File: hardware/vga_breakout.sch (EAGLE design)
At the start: 11 parts, among them J1 VGA_DB15, J2 HEADER_5P

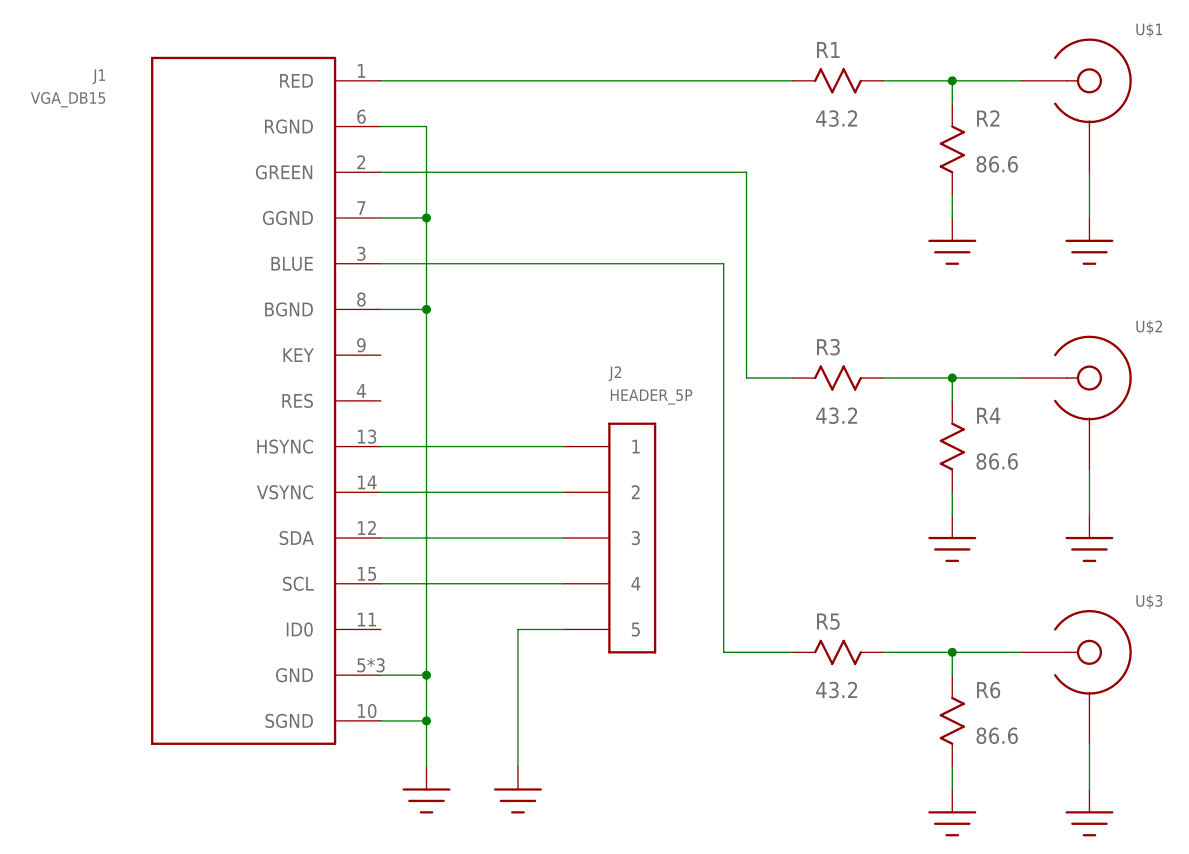
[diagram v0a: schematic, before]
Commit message: added +5V line to breakout PCB
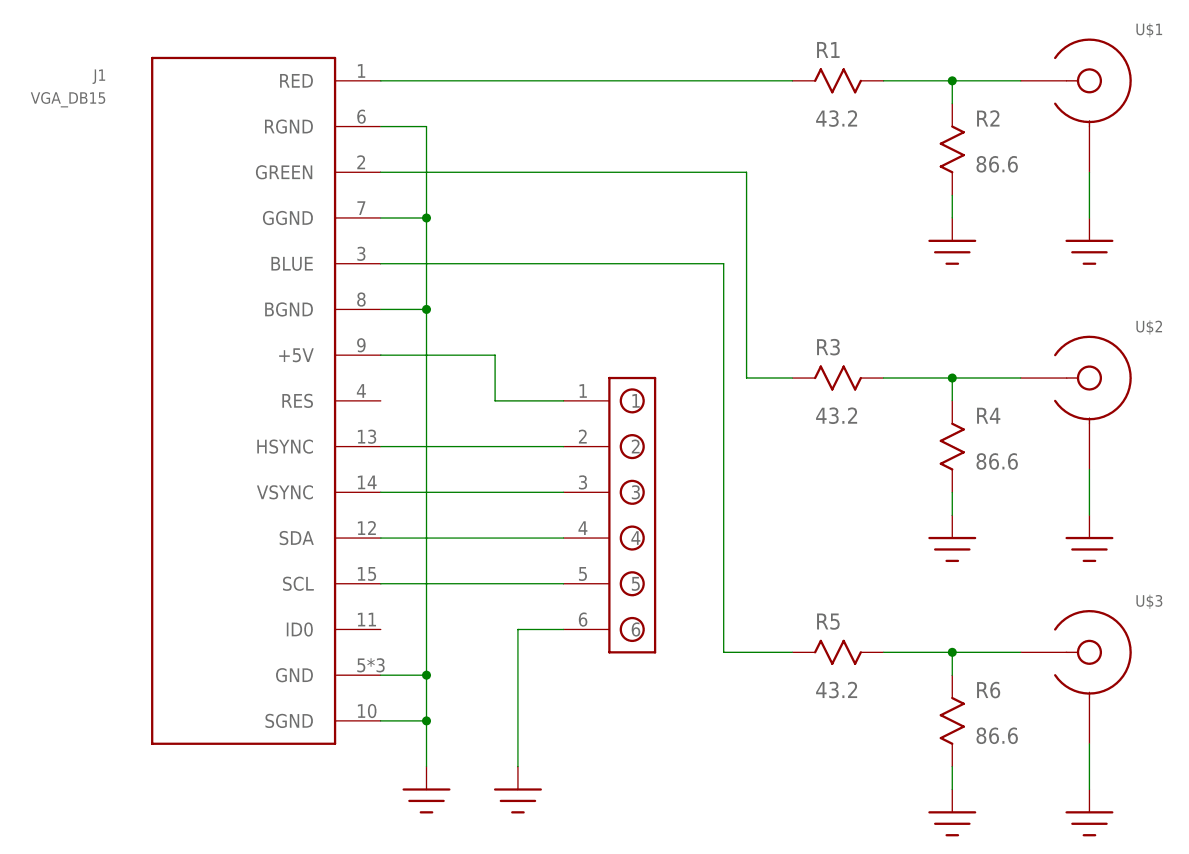
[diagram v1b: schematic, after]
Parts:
- removed J2: HEADER_5P, mw-voice-marker:HEADER_5P
- added U$9: HEADER_6P, mw-voice-marker:HEADER_6P
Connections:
- new net +5V: J1.+5V, U$9.1
- net GND: now also U$9.6; no longer J2.5
- net HSYNC: now also U$9.2; no longer J2.1
- net SCL: now also U$9.5; no longer J2.4
- net SDA: now also U$9.4; no longer J2.3
- net VSYNC: now also U$9.3; no longer J2.2
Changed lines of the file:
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@@
 <part name="U$16" library="mw-voice-marker" deviceset="GND" device=""/>
 <part name="U$17" library="mw-voice-marker" deviceset="GND" device=""/>
-<part name="J2" library="mw-voice-marker" deviceset="HEADER_5P" device=""/>
+<part name="U$9" library="mw-voice-marker" deviceset="HEADER_6P" device=""/>
 </parts>
 <sheets>
@@
 <instance part="U$16" gate="G$1" x="71.12" y="40.64"/>
 <instance part="U$17" gate="G$1" x="71.12" y="10.16"/>
-<instance part="J2" gate="G$1" x="35.56" y="38.1"/>
+<instance part="U$9" gate="G$1" x="33.02" y="40.64"/>
 </instances>
 <busses>
@@
 <pinref part="U$8" gate="G$1" pin="GND"/>
 <wire x1="22.86" y1="27.94" x2="22.86" y2="12.7" width="0.1524" layer="91"/>
-<pinref part="J2" gate="G$1" pin="5"/>
 <wire x1="22.86" y1="27.94" x2="27.94" y2="27.94" width="0.1524" layer="91"/>
+<pinref part="U$9" gate="G$1" pin="6"/>
 </segment>
 <segment>
@@
 <pinref part="J1" gate="G$1" pin="SDA"/>
 <wire x1="7.62" y1="38.1" x2="27.94" y2="38.1" width="0.1524" layer="91"/>
-<pinref part="J2" gate="G$1" pin="3"/>
+<pinref part="U$9" gate="G$1" pin="4"/>
 </segment>
 </net>
@@
 <pinref part="J1" gate="G$1" pin="SCL"/>
 <wire x1="7.62" y1="33.02" x2="27.94" y2="33.02" width="0.1524" layer="91"/>
-<pinref part="J2" gate="G$1" pin="4"/>
+<pinref part="U$9" gate="G$1" pin="5"/>
 </segment>
 </net>
@@
 <net name="VSYNC" class="0">
 <segment>
-<pinref part="J2" gate="G$1" pin="2"/>
 <pinref part="J1" gate="G$1" pin="VSYNC"/>
 <wire x1="27.94" y1="43.18" x2="7.62" y2="43.18" width="0.1524" layer="91"/>
+<pinref part="U$9" gate="G$1" pin="3"/>
 </segment>
 </net>
@@
 <segment>
 <pinref part="J1" gate="G$1" pin="HSYNC"/>
-<pinref part="J2" gate="G$1" pin="1"/>
 <wire x1="7.62" y1="48.26" x2="27.94" y2="48.26" width="0.1524" layer="91"/>
-</segment>
-</net>
+<pinref part="U$9" gate="G$1" pin="2"/>
+</segment>
+</net>
+<net name="+5V" class="0">
+<segment>
+<pinref part="U$9" gate="G$1" pin="1"/>
+<wire x1="27.94" y1="53.34" x2="20.32" y2="53.34" width="0.1524" layer="91"/>
+<wire x1="20.32" y1="53.34" x2="20.32" y2="58.42" width="0.1524" layer="91"/>
+<pinref part="J1" gate="G$1" pin="+5V"/>
+<wire x1="20.32" y1="58.42" x2="7.62" y2="58.42" width="0.1524" layer="91"/>
+</segment>
+</net>
